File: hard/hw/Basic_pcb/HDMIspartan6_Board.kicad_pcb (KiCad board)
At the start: 4 copper layers, 53.3 x 85.1 mm, 164 parts, among them IC1 W9812G6KH, J1 HDMI_A, J2 CONN_3X1F, P1 CONN_01X03, P2 CONN_01X02, P3 CONN_02X02, P4 CONN_02X02, P5 CONN_01X03, SW1 B3SL-1002P, U1 PAM8302AASCR, U2 TPS63070, X1 ASV-32.000MHZ-E-T

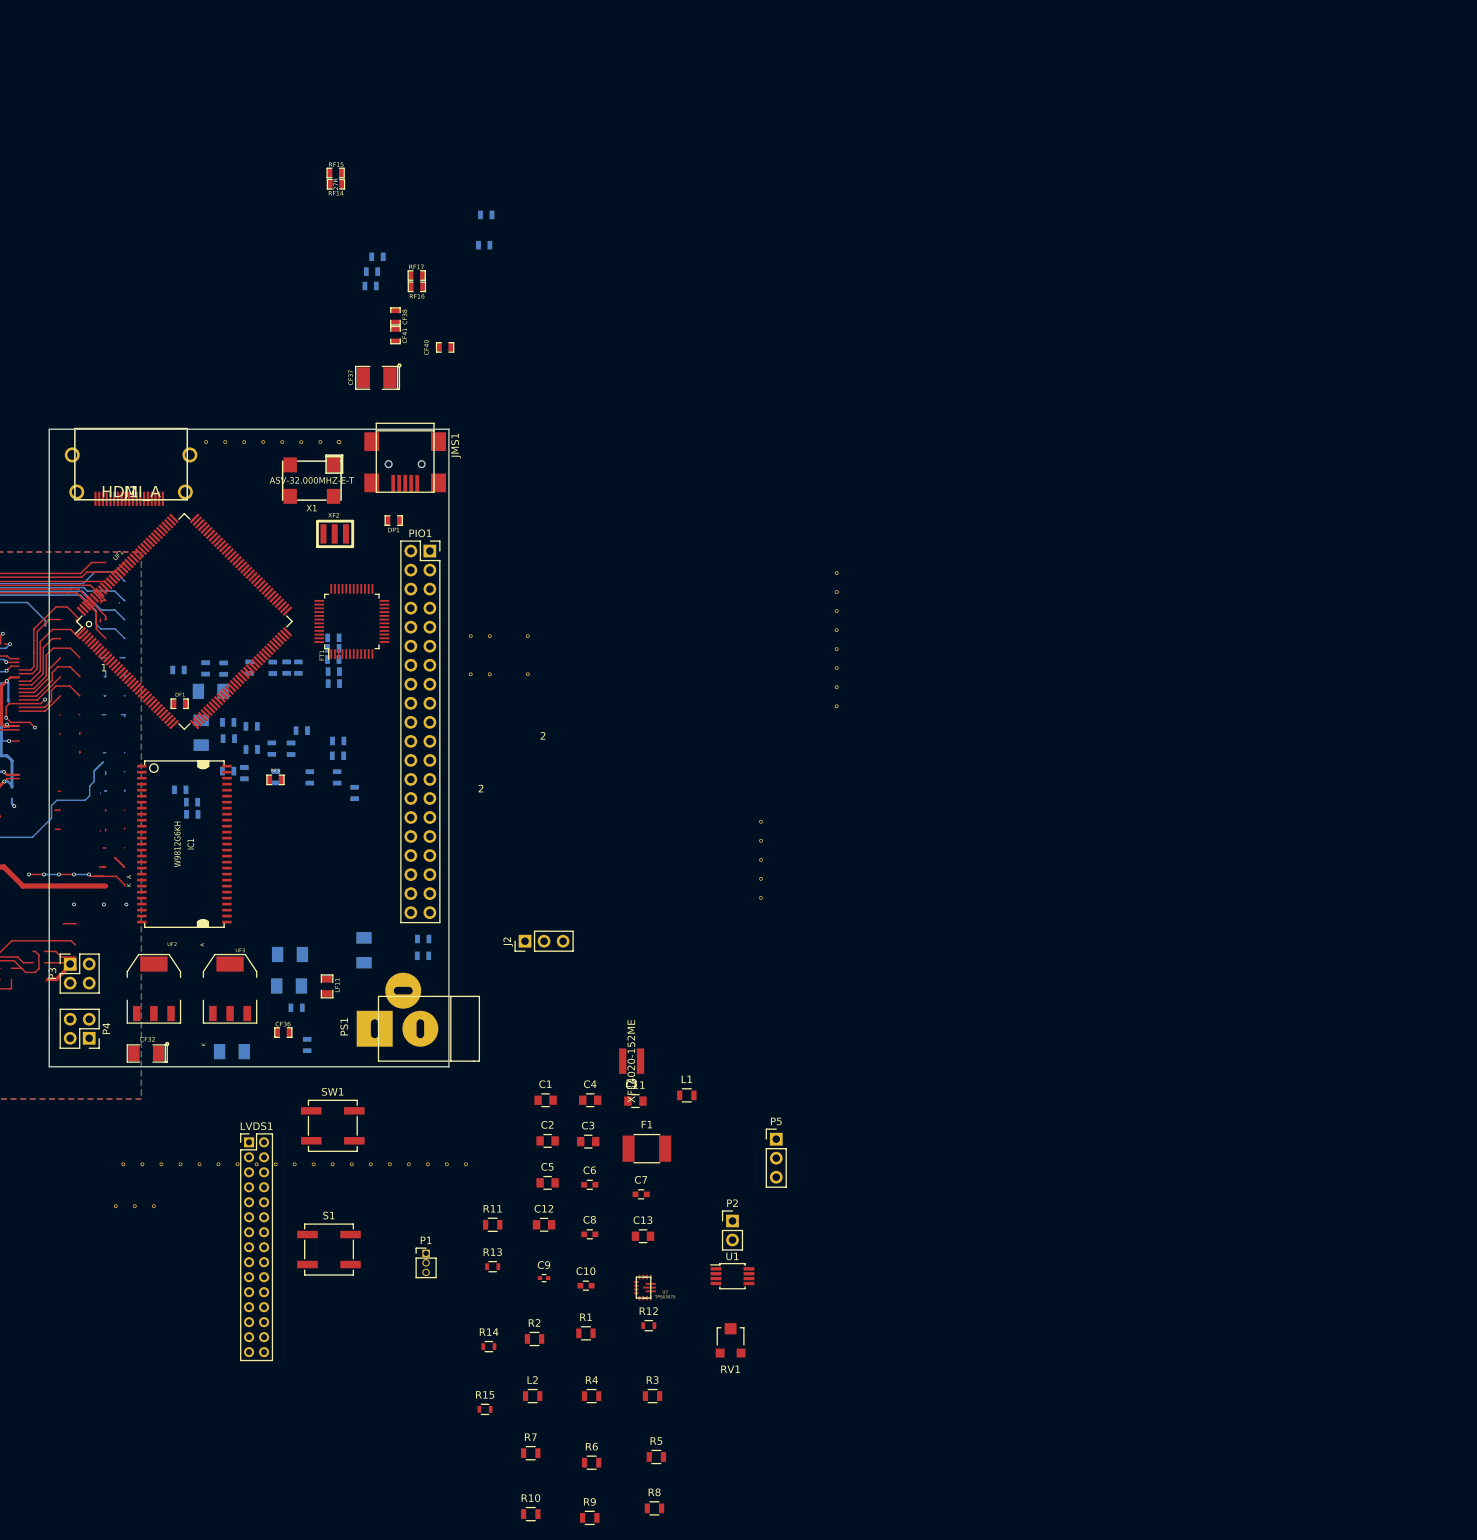
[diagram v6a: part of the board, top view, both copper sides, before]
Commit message: Alimentacion Pantalla
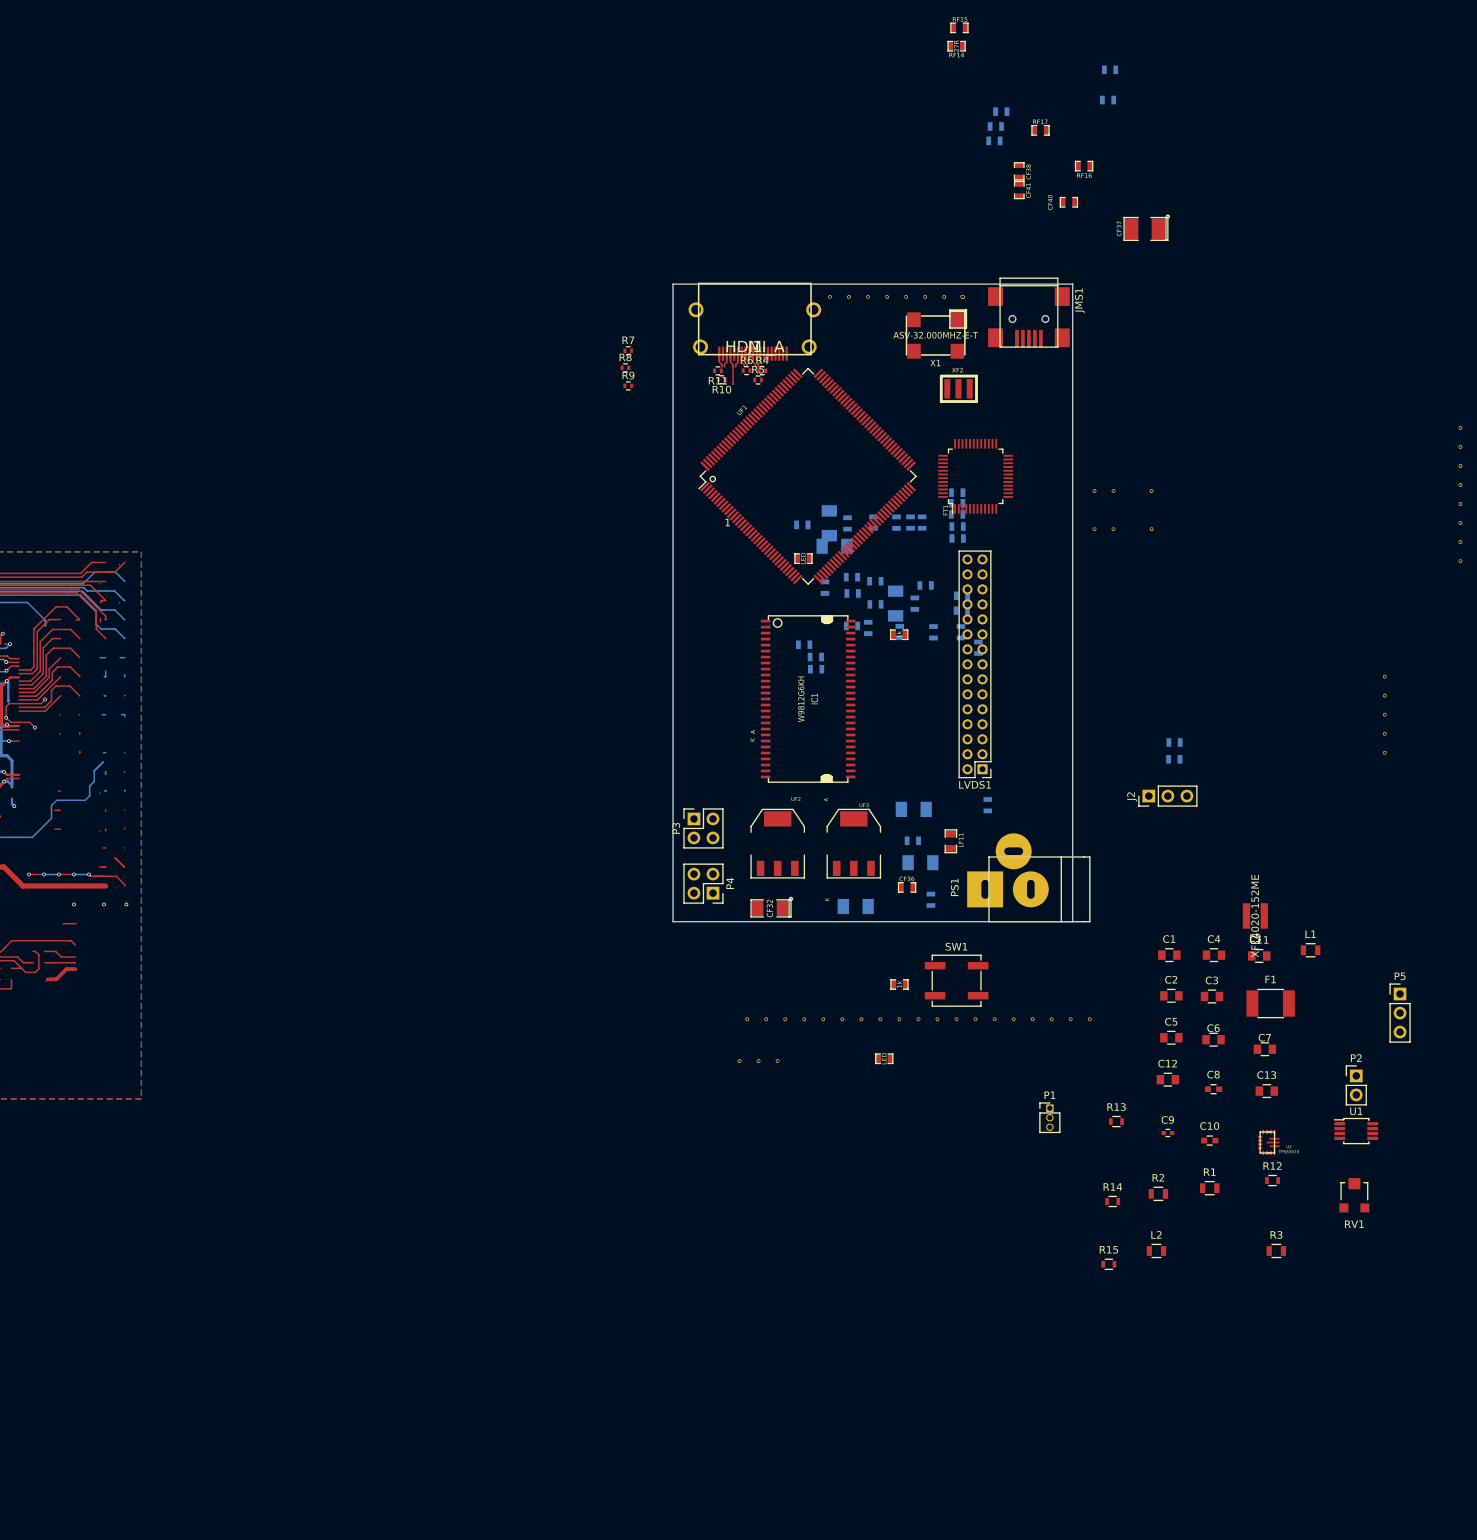
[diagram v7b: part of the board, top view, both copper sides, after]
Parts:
- removed DP1: DIODE, opendous:SM0603_Opendous
- removed PIO1: CONN_02X20, Socket_Strips:Socket_Strip_Straight_2x20_Pitch2.54mm
- removed S1: B3SL-1002P, Buttons_Switches_SMD:SW_SPST_B3SL-1002P
- added DF2: LED, opendous:SM0603, F.Cu at (191.4, 133.9)
- added RF8: 1k, opendous:SM0603, F.Cu at (193.5, 124.0)
- C6, C7: footprint Capacitors_SMD:C_0603 -> Capacitors_SMD:C_0805
- CF1, CF10, CF11, CF12, CF14, CF16, CF17, CF18, CF19, CF2, CF20, CF21, CF23, CF24, CF25, CF26, CF27, CF3, CF31, CF4, CF5, CF6, CF7, CF8, CF9, DF1, RF1, RF2, RF3, RF4, RF5, RF6, RF7: footprint SM0603 -> opendous:SM0603
- CF13, CF28, CF33: footprint SM0603 -> opendous:SM1206_Opendous
- CF15, CF22, CF34: footprint SM1206_Opendous -> opendous:SM0603
- CF29, CF30, CF32, CF35: footprint SM1206_Opendous -> opendous:SM1206_Opendous
- R10, R11, R4, R5, R6, R7, R8, R9: footprint Resistors_SMD:R_0805 -> Resistors_SMD:R_0402
- moved R10 153.5 mm to (169.8, 43.3), turned to 180 degrees
- moved R8 152.3 mm to (156.9, 41.7)
- moved R9 151.2 mm to (157.3, 44.2)
- moved R7 147.7 mm to (157.3, 39.5)
- moved R6 147.2 mm to (173.1, 42.1)
- moved R5 144.4 mm to (174.6, 43.4)
- moved R4 138.7 mm to (175.2, 42.1)
- moved R11 117.9 mm to (169.2, 42.1), turned to 180 degrees
- moved LVDS1 109.8 mm to (204.5, 95.3), turned to 180 degrees
- moved CF37 104.5 mm to (226.2, 23.2)
- moved CF26 103.6 mm to (230.1, 94.0)
- moved CF8 103.6 mm to (230.2, 91.7)
- moved RF16 90.5 mm to (218.1, 14.8)
- moved C10 85.5 mm to (234.9, 144.9)
- moved C11 85.5 mm to (241.5, 120.2)
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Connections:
- DF1 pad 1: /spartan6/IO_LED -> Net-(DF1-Pad1)
- R1 pad 2: Net-(R1-Pad2) -> +5V
- UF1 pad 100: /spartan6/IO25 -> Net-(UF1-Pad100)
- UF1 pad 102: /spartan6/IO26 -> Net-(UF1-Pad102)
- UF1 pad 104: /spartan6/IO27 -> Net-(UF1-Pad104)
- UF1 pad 116: /spartan6/IO28 -> Net-(UF1-Pad116)
- UF1 pad 117: /spartan6/IO29 -> Net-(UF1-Pad117)
- UF1 pad 120: /spartan6/IO30 -> Net-(UF1-Pad120)
- UF1 pad 121: /spartan6/IO31 -> Net-(UF1-Pad121)
- UF1 pad 123: /spartan6/IO32 -> Net-(UF1-Pad123)
- UF1 pad 124: /spartan6/IO33 -> Net-(UF1-Pad124)
- UF1 pad 126: /spartan6/IO34 -> Net-(UF1-Pad126)
- UF1 pad 127: /spartan6/IO35 -> Net-(UF1-Pad127)
- UF1 pad 131: /spartan6/IO36 -> Net-(UF1-Pad131)
- UF1 pad 132: /spartan6/IO37 -> Net-(UF1-Pad132)
- UF1 pad 39: /spartan6/IO01 -> Net-(UF1-Pad39)
- UF1 pad 47: /spartan6/IO02 -> Net-(UF1-Pad47)
- UF1 pad 48: /spartan6/IO03 -> Net-(UF1-Pad48)
- UF1 pad 59: /spartan6/IO_LED -> Net-(UF1-Pad59)
- UF1 pad 66: /spartan6/IO04 -> Net-(UF1-Pad66)
- UF1 pad 67: /spartan6/IO05 -> Net-(UF1-Pad67)
- UF1 pad 70: +3V3 -> Net-(UF1-Pad70)
- UF1 pad 74: /spartan6/IO07 -> Net-(UF1-Pad74)
- UF1 pad 75: /spartan6/IO08 -> Net-(UF1-Pad75)
- UF1 pad 78: /spartan6/IO09 -> Net-(UF1-Pad78)
- UF1 pad 79: /spartan6/IO10 -> Net-(UF1-Pad79)
- UF1 pad 80: /spartan6/IO11 -> Net-(UF1-Pad80)
- UF1 pad 81: /spartan6/IO12 -> Net-(UF1-Pad81)
- UF1 pad 82: /spartan6/IO13 -> Net-(UF1-Pad82)
- UF1 pad 83: /spartan6/IO14 -> Net-(UF1-Pad83)
- UF1 pad 84: /spartan6/IO15 -> Net-(UF1-Pad84)
- UF1 pad 85: /spartan6/IO16 -> Net-(UF1-Pad85)
- UF1 pad 87: /spartan6/IO17 -> Net-(UF1-Pad87)
- UF1 pad 88: /spartan6/IO18 -> Net-(UF1-Pad88)
- UF1 pad 92: /spartan6/IO19 -> Net-(UF1-Pad92)
- UF1 pad 93: /spartan6/IO20 -> Net-(UF1-Pad93)
- UF1 pad 95: /spartan6/IO21 -> Net-(UF1-Pad95)
- UF1 pad 97: /spartan6/IO22 -> Net-(UF1-Pad97)
- UF1 pad 98: /spartan6/IO23 -> Net-(UF1-Pad98)
- UF1 pad 99: /spartan6/IO24 -> Net-(UF1-Pad99)
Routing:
- net (no net): track 3259.9 -> 3334.6 mm
- net GND: track 35.1 -> 0.00 mm
- net /spartan6/TMDS_CLK_P: track 30.8 -> 1.88 mm
- net +3V3: track 8.73 -> 0.00 mm
- net /spartan6/TMDS_D1_P: track 0.00 -> 4.17 mm
- net /spartan6/TMDS_D2_P: track 0.00 -> 1.89 mm
- net /spartan6/TMDS_D1_N: track 0.00 -> 1.87 mm
- net /spartan6/TMDS_D0_P: track 0.00 -> 1.87 mm
- net /spartan6/TMDS_D2_N: track 0.00 -> 1.86 mm
- net /spartan6/TMDS_CLK_N: track 0.00 -> 1.86 mm
- net /spartan6/TMDS_D0_N: track 0.00 -> 1.85 mm
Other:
- board text removed: "2"

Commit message: Todos los componentes en la tarjeta
by Ruben
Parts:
- removed J2: CONN_3X1F, Socket_Strips:Socket_Strip_Straight_1x03_Pitch2.54mm
- added P7: B6B-PH-K-S(LF)(SN), Connectors_JST:JST_PH_B6B-PH-K_06x2.00mm_Straight, F.Cu at (92.1, 86.5)
- added S1: 9077-1, resonator:CKCOMP-OS102011MA1QN1, F.Cu at (109.3, 95.3)
- CF32, CF36, DF1, F1, FT1, LF11, RF5: moved to B.Cu
- moved P5 203.8 mm to (60.4, 85.5), turned to 90 degrees
- moved L2 199.3 mm to (39.7, 93.6)
- moved RV1 199.2 mm to (64.8, 90.7)
- moved R3 198.1 mm to (52.1, 109.7)
- moved P2 197.8 mm to (60.4, 97.6)
- moved L1 197.0 mm to (52.4, 98.7)
- moved U1 194.9 mm to (64.9, 98.2), turned to 270 degrees
- moved R1 194.8 mm to (45.5, 105.9)
- moved C3 192.3 mm to (45.7, 92.5)
- moved C4 190.5 mm to (46.2, 97.8)
- moved C2 185.3 mm to (46.0, 101.7)
- moved R2 182.3 mm to (51.7, 105.9)
- moved C5 181.1 mm to (52.6, 93.6)
- moved C1 178.4 mm to (51.9, 103.0)
- moved R12 171.2 mm to (74.7, 120.5)
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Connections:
- C6 pad 1: +9V -> /Power/+9V0
- C7 pad 1: +9V -> /Power/+9V0
- C8 pad 1: +9V -> /Power/+9V0
- R12 pad 1: +9V -> /Power/+9V0
- U2 pad 12: +9V -> /Power/+9V0
- U2 pad 13: +9V -> /Power/+9V0
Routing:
- net (no net): track 3334.6 -> 0.00 mm, vias 179 -> 0
- net /spartan6/TMDS_D1_P: track 4.17 -> 0.00 mm
- net /spartan6/TMDS_D2_P: track 1.89 -> 0.00 mm
- net /spartan6/TMDS_CLK_P: track 1.88 -> 0.00 mm
- net /spartan6/TMDS_D1_N: track 1.87 -> 0.00 mm
- net /spartan6/TMDS_D0_P: track 1.87 -> 0.00 mm
- net /spartan6/TMDS_D2_N: track 1.86 -> 0.00 mm
- net /spartan6/TMDS_CLK_N: track 1.86 -> 0.00 mm
- net /spartan6/TMDS_D0_N: track 1.85 -> 0.00 mm
- removed copper zone on B.Cu, net GND
- removed copper zone on F.Cu, net GND
